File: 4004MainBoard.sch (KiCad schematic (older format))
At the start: 94 parts, among them J1 BUS, J2 P0 RAM1, J3 CMRAM RAM2, J4 P0 RAM2, J5 DC 5V, Q1 2SA1162GR, Q10 2SC2712GR, Q11 2SA1162GR, Q2 2SC2712GR, Q3 2SA1162GR, Q4 2SC2712GR, Q5 2SA1162GR, Q6 2SA1162GR, Q7 2SA1162GR, Q8 2SA1162GR, Q9 2SC2712GR, SW1 TEST, SW2 RESET, SW3 POWER, U1 74HC08, U2 74HC161, U3 PST600, U4 Intel4004, U5 LT1931A, U6 74LS540, U7 Intel4002-1, U8 Intel4002-1, U9 LT1763, Y1 DLO555MB

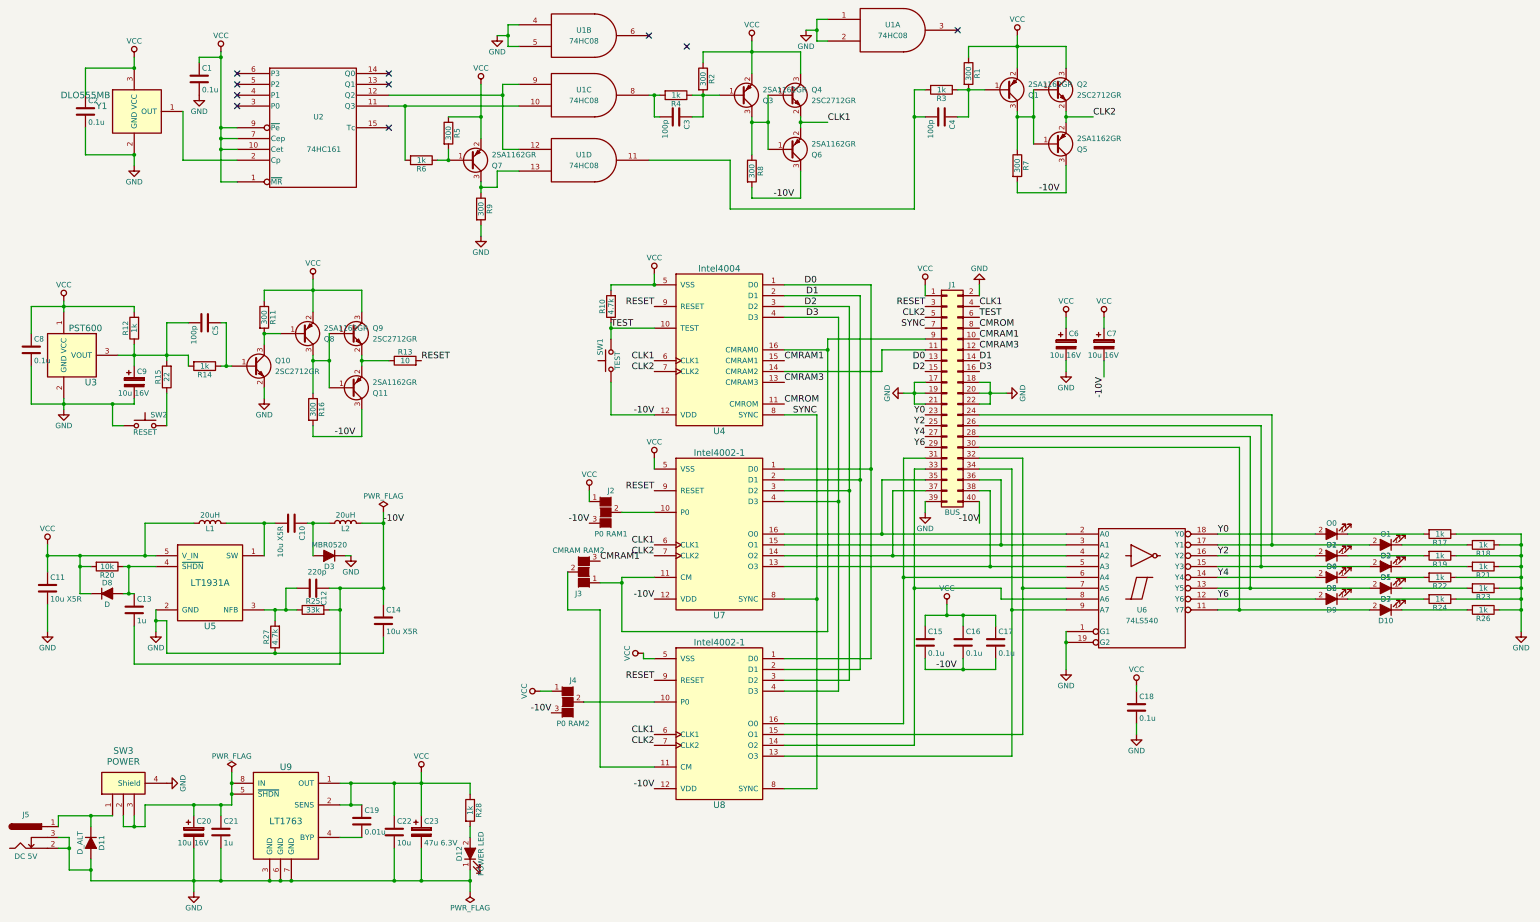
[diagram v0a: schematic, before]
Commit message: パターンを実装
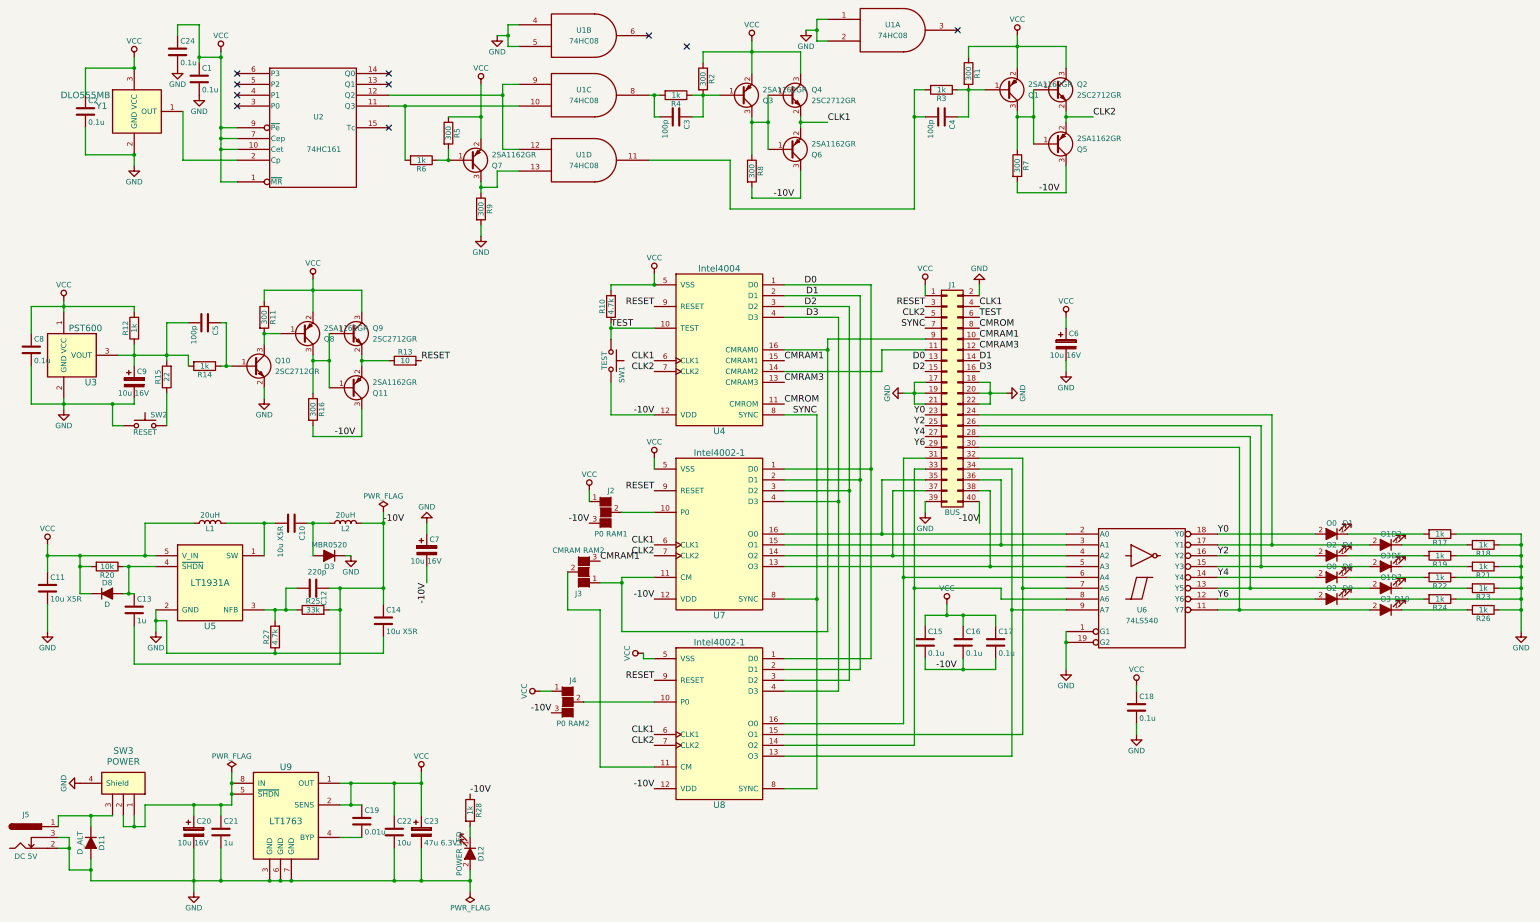
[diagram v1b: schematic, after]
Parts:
- added C24: 0.1u, Capacitors_SMD:C_0603_HandSoldering, symbol C
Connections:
- net -10V: now also R28.1, SW1.2; no longer SW1.1
- net GND: now also C7.1, D12.2 (A), C24.2; no longer D12.1 (K)
- net TEST: now also SW1.1; no longer SW1.2
- net VCC: now also C24.1; no longer C7.1, R28.1
- net at D11.1 (K), J5.1: now also SW3.3; no longer SW3.1
- net at C20.1, C21.1, SW3.2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: now also SW3.1; no longer SW3.3
- net at R28.2: now also D12.1 (K); no longer D12.2 (A)
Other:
- moved on the sheet: C7, D12, SW1, SW3
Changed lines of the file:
@@
 F 3 "" H 2000 8300 60  0001 C CNN
 	1    2000 8300
-	1    0    0    -1
+	-1   0    0    -1
 $EndComp
 $Comp
@@
 L GND #PWR02
 U 1 1 5A62F813
-P 2400 8200
-F 0 "#PWR02" H 2400 7950 50  0001 C CNN
-F 1 "GND" H 2400 8050 50  0000 C CNN
-F 2 "" H 2400 8200 50  0001 C CNN
-F 3 "" H 2400 8200 50  0001 C CNN
-	1    2400 8200
-	0    -1   -1   0
+P 1600 8200
+F 0 "#PWR02" H 1600 7950 50  0001 C CNN
+F 1 "GND" H 1600 8050 50  0000 C CNN
+F 2 "" H 1600 8200 50  0001 C CNN
+F 3 "" H 1600 8200 50  0001 C CNN
+	1    1600 8200
+	0    1    1    0
 $EndComp
 $Comp
@@
 F 3 "" H 5200 8850 50  0001 C CNN
 	1    5200 8850
-	0    -1   -1   0
+	0    1    1    0
 $EndComp
 $Comp
@@
 F 3 "" H 6500 4500 50  0001 C CNN
 	1    6500 4300
-	0    -1   -1   0
+	0    1    1    0
 $EndComp
 Text Label 6500 4000 0    60   ~ 0
@@
 Connection ~ 4500 9100
 Wire Wire Line
-	4000 8200 5200 8200
+	4000 8200 4750 8200
 Wire Wire Line
 	4500 8200 4500 8500
@@
 Wire Wire Line
 	5200 8700 5200 8600
-Wire Wire Line
-	5200 8200 5200 8300
 Wire Wire Line
 	2300 6600 2300 6800
@@
 Connection ~ 2900 2350
 Wire Wire Line
-	2700 1550 2700 1500
+	2700 1200 2700 1550
 Wire Wire Line
 	2700 1500 2900 1500
@@
 U 1 1 5A66297C
 P 13150 5900
-F 0 "D1" H 13150 6000 50  0000 C CNN
+F 0 "D1" H 13000 5800 50  0000 C CNN
 F 1 "O0" H 13150 5800 50  0000 C CNN
 F 2 "LEDs:LED_0603_HandSoldering" H 13150 5900 50  0001 C CNN
@@
 U 1 1 5A662D8D
 P 13150 6100
-F 0 "D4" H 13150 6200 50  0000 C CNN
+F 0 "D4" H 13000 6000 50  0000 C CNN
 F 1 "O2" H 13150 6000 50  0000 C CNN
 F 2 "LEDs:LED_0603_HandSoldering" H 13150 6100 50  0001 C CNN
@@
 U 1 1 5A662EAB
 P 13150 6300
-F 0 "D6" H 13150 6400 50  0000 C CNN
+F 0 "D6" H 13000 6200 50  0000 C CNN
 F 1 "O0" H 13150 6200 50  0000 C CNN
 F 2 "LEDs:LED_0603_HandSoldering" H 13150 6300 50  0001 C CNN
@@
 U 1 1 5A662FC5
 P 13150 6500
-F 0 "D9" H 13150 6600 50  0000 C CNN
+F 0 "D9" H 13000 6400 50  0000 C CNN
 F 1 "O2" H 13150 6400 50  0000 C CNN
 F 2 "LEDs:LED_0603_HandSoldering" H 13150 6500 50  0001 C CNN
@@
 U 1 1 5A663256
 P 13650 6000
-F 0 "D2" H 13650 6100 50  0000 C CNN
+F 0 "D2" H 13550 5900 50  0000 C CNN
 F 1 "O1" H 13650 5900 50  0000 C CNN
 F 2 "LEDs:LED_0603_HandSoldering" H 13650 6000 50  0001 C CNN
@@
 U 1 1 5A66337A
 P 13650 6200
-F 0 "D5" H 13650 6300 50  0000 C CNN
+F 0 "D5" H 13550 6100 50  0000 C CNN
 F 1 "O3" H 13650 6100 50  0000 C CNN
 F 2 "LEDs:LED_0603_HandSoldering" H 13650 6200 50  0001 C CNN
@@
 U 1 1 5A66349C
 P 13650 6400
-F 0 "D7" H 13650 6500 50  0000 C CNN
+F 0 "D7" H 13550 6300 50  0000 C CNN
 F 1 "O1" H 13650 6300 50  0000 C CNN
 F 2 "LEDs:LED_0603_HandSoldering" H 13650 6400 50  0001 C CNN
@@
 U 1 1 5A6635C2
 P 13650 6600
-F 0 "D10" H 13650 6700 50  0000 C CNN
+F 0 "D10" H 13500 6500 50  0000 C CNN
 F 1 "O3" H 13650 6500 50  0000 C CNN
 F 2 "LEDs:LED_0603_HandSoldering" H 13650 6600 50  0001 C CNN
@@
 L CP C7
 U 1 1 5A66BB0D
-P 11050 4150
-F 0 "C7" H 11075 4250 50  0000 L CNN
-F 1 "10u 16V" H 10900 4050 50  0000 L CNN
-F 2 "Capacitors_SMD:CP_Elec_4x4.5" H 11088 4000 50  0001 C CNN
-F 3 "" H 11050 4150 50  0001 C CNN
-	1    11050 4150
-	1    0    0    -1
-$EndComp
-$Comp
-L VCC #PWR037
-U 1 1 5A66BC40
-P 11050 3900
-F 0 "#PWR037" H 11050 3750 50  0001 C CNN
-F 1 "VCC" H 11050 4050 50  0000 C CNN
-F 2 "" H 11050 3900 50  0001 C CNN
-F 3 "" H 11050 3900 50  0001 C CNN
-	1    11050 3900
-	1    0    0    -1
-$EndComp
-Text Label 11050 4450 3    60   ~ 0
+P 4800 6050
+F 0 "C7" H 4825 6150 50  0000 L CNN
+F 1 "10u 16V" H 4650 5950 50  0000 L CNN
+F 2 "Capacitors_SMD:CP_Elec_4x4.5" H 4838 5900 50  0001 C CNN
+F 3 "" H 4800 6050 50  0001 C CNN
+	1    4800 6050
+	1    0    0    -1
+$EndComp
+Text Label 4800 6350 3    60   ~ 0
 -10V
 Wire Wire Line
-	11050 4300 11050 4450
-Wire Wire Line
-	11050 4000 11050 3900
-$Comp
-L PWR_FLAG #FLG038
+	4800 6200 4800 6350
+Wire Wire Line
+	4800 5900 4800 5800
+$Comp
+L PWR_FLAG #FLG037
 U 1 1 5A66F18F
 P 5200 9200
-F 0 "#FLG038" H 5200 9275 50  0001 C CNN
+F 0 "#FLG037" H 5200 9275 50  0001 C CNN
 F 1 "PWR_FLAG" H 5200 9350 50  0000 C CNN
 F 2 "" H 5200 9200 50  0001 C CNN
@@
 $EndComp
 $Comp
-L PWR_FLAG #FLG039
+L PWR_FLAG #FLG038
 U 1 1 5A66F31E
 P 4400 5700
-F 0 "#FLG039" H 4400 5775 50  0001 C CNN
+F 0 "#FLG038" H 4400 5775 50  0001 C CNN
 F 1 "PWR_FLAG" H 4400 5850 50  0000 C CNN
 F 2 "" H 4400 5700 50  0001 C CNN
@@
 Connection ~ 5200 9100
 $Comp
-L PWR_FLAG #FLG040
+L PWR_FLAG #FLG039
 U 1 1 5A66FDA3
 P 3000 8100
-F 0 "#FLG040" H 3000 8175 50  0001 C CNN
+F 0 "#FLG039" H 3000 8175 50  0001 C CNN
 F 1 "PWR_FLAG" H 3000 8250 50  0000 C CNN
 F 2 "" H 3000 8100 50  0001 C CNN
@@
 Connection ~ 10000 4600
 $Comp
-L GND #PWR041
+L GND #PWR040
 U 1 1 5A67152F
 P 9200 4600
-F 0 "#PWR041" H 9200 4350 50  0001 C CNN
+F 0 "#PWR040" H 9200 4350 50  0001 C CNN
 F 1 "GND" H 9200 4450 50  0000 C CNN
 F 2 "" H 9200 4600 50  0001 C CNN
@@
 $EndComp
 $Comp
-L GND #PWR042
+L GND #PWR041
 U 1 1 5A67165D
 P 10150 4600
-F 0 "#PWR042" H 10150 4350 50  0001 C CNN
+F 0 "#PWR041" H 10150 4350 50  0001 C CNN
 F 1 "GND" H 10150 4450 50  0000 C CNN
 F 2 "" H 10150 4600 50  0001 C CNN
@@
 	0    -1   -1   0
 $EndComp
+$Comp
+L GND #PWR042
+U 1 1 5A6475BE
+P 4800 5800
+F 0 "#PWR042" H 4800 5550 50  0001 C CNN
+F 1 "GND" H 4800 5650 50  0000 C CNN
+F 2 "" H 4800 5800 50  0001 C CNN
+F 3 "" H 4800 5800 50  0001 C CNN
+	1    4800 5800
+	-1   0    0    1
+$EndComp
+$Comp
+L C C24
+U 1 1 5A648DDE
+P 2500 1450
+F 0 "C24" H 2525 1550 50  0000 L CNN
+F 1 "0.1u" H 2525 1350 50  0000 L CNN
+F 2 "Capacitors_SMD:C_0603_HandSoldering" H 2538 1300 50  0001 C CNN
+F 3 "" H 2500 1450 50  0001 C CNN
+	1    2500 1450
+	1    0    0    -1
+$EndComp
+$Comp
+L GND #PWR043
+U 1 1 5A649039
+P 2500 1600
+F 0 "#PWR043" H 2500 1350 50  0001 C CNN
+F 1 "GND" H 2500 1450 50  0000 C CNN
+F 2 "" H 2500 1600 50  0001 C CNN
+F 3 "" H 2500 1600 50  0001 C CNN
+	1    2500 1600
+	1    0    0    -1
+$EndComp
+Wire Wire Line
+	2500 1300 2500 1200
+Wire Wire Line
+	2500 1200 2700 1200
+Connection ~ 2700 1500
+Text Label 5200 8300 0    60   ~ 0
+-10V
 $EndSCHEMATC

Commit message: パターン修正 ビア実装
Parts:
- added R29, R30: 22, Resistors_SMD:R_0603_HandSoldering, symbol R
- added R31, R32, R33, R34: 22k, Resistors_SMD:R_0603_HandSoldering, symbol R
- D12: value POWER LED -> POWER
- R13: value 10 -> 22
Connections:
- net CLK1: now also R30.2; no longer Q4.2 (E), Q6.2 (E)
- net CLK2: now also R29.2; no longer Q2.2 (E), Q5.2 (E)
- net D0: now also R34.2
- net D1: now also R33.2
- net D2: now also R32.2
- net D3: now also R31.2
- net VCC: now also R31.1, R32.1, R33.1, R34.1
- new net: Q4.2 (E), Q6.2 (E), R30.1
- new net: Q2.2 (E), Q5.2 (E), R29.1
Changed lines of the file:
@@
 P 5200 8850
 F 0 "D12" H 5200 8950 50  0000 C CNN
-F 1 "POWER LED" H 5200 8750 50  0000 C CNN
+F 1 "POWER" H 5200 8750 50  0000 C CNN
 F 2 "LEDs:LED_0603_HandSoldering" H 5200 8850 50  0001 C CNN
 F 3 "" H 5200 8850 50  0001 C CNN
@@
 Text Label 8000 2800 0    60   ~ 0
 -10V
-Text Label 8500 2100 0    60   ~ 0
+Text Label 8800 2100 0    60   ~ 0
 CLK1
 $Comp
@@
 Text Label 10450 2750 0    60   ~ 0
 -10V
-Text Label 10950 2050 0    60   ~ 0
+Text Label 11250 2050 0    60   ~ 0
 CLK2
 Text Label 4750 4300 0    60   ~ 0
@@
 P 4600 4300
 F 0 "R13" V 4680 4300 50  0000 C CNN
-F 1 "10" V 4600 4300 50  0000 C CNN
+F 1 "22" V 4600 4300 50  0000 C CNN
 F 2 "Resistors_SMD:R_0603_HandSoldering" V 4530 4300 50  0001 C CNN
 F 3 "" H 4600 4300 50  0001 C CNN
@@
 	8100 3900 8600 3900
 Wire Wire Line
-	8600 3900 8600 7350
+	8600 3500 8600 7350
 Wire Wire Line
 	8600 5600 8100 5600
@@
 	8100 5500 8700 5500
 Wire Wire Line
-	8700 3800 8700 7250
+	8700 3500 8700 7250
 Wire Wire Line
 	8700 3800 8100 3800
@@
 	8100 5400 8800 5400
 Wire Wire Line
-	8800 3700 8800 7150
+	8800 3500 8800 7150
 Wire Wire Line
 	8800 3700 8100 3700
@@
 	8100 5300 8900 5300
 Wire Wire Line
-	8900 3600 8900 7050
+	8900 3500 8900 7050
 Wire Wire Line
 	8900 3600 8100 3600
@@
 Text Label 5200 8300 0    60   ~ 0
 -10V
+$Comp
+L R R30
+U 1 1 5AEC6C94
+P 8650 2100
+F 0 "R30" V 8730 2100 50  0000 C CNN
+F 1 "22" V 8650 2100 50  0000 C CNN
+F 2 "Resistors_SMD:R_0603_HandSoldering" V 8580 2100 50  0001 C CNN
+F 3 "" H 8650 2100 50  0001 C CNN
+	1    8650 2100
+	0    -1   -1   0
+$EndComp
+$Comp
+L R R29
+U 1 1 5AEC6F5E
+P 11100 2050
+F 0 "R29" V 11180 2050 50  0000 C CNN
+F 1 "22" V 11100 2050 50  0000 C CNN
+F 2 "Resistors_SMD:R_0603_HandSoldering" V 11030 2050 50  0001 C CNN
+F 3 "" H 11100 2050 50  0001 C CNN
+	1    11100 2050
+	0    -1   -1   0
+$EndComp
+$Comp
+L R R31
+U 1 1 5AEC8B2E
+P 8600 3350
+F 0 "R31" V 8680 3350 50  0000 C CNN
+F 1 "22k" V 8600 3350 50  0000 C CNN
+F 2 "Resistors_SMD:R_0603_HandSoldering" V 8530 3350 50  0001 C CNN
+F 3 "" H 8600 3350 50  0001 C CNN
+	1    8600 3350
+	1    0    0    -1
+$EndComp
+$Comp
+L R R32
+U 1 1 5AEC8D49
+P 8700 3350
+F 0 "R32" V 8780 3350 50  0000 C CNN
+F 1 "22k" V 8700 3350 50  0000 C CNN
+F 2 "Resistors_SMD:R_0603_HandSoldering" V 8630 3350 50  0001 C CNN
+F 3 "" H 8700 3350 50  0001 C CNN
+	1    8700 3350
+	1    0    0    -1
+$EndComp
+$Comp
+L R R33
+U 1 1 5AEC8E8A
+P 8800 3350
+F 0 "R33" V 8880 3350 50  0000 C CNN
+F 1 "22k" V 8800 3350 50  0000 C CNN
+F 2 "Resistors_SMD:R_0603_HandSoldering" V 8730 3350 50  0001 C CNN
+F 3 "" H 8800 3350 50  0001 C CNN
+	1    8800 3350
+	1    0    0    -1
+$EndComp
+$Comp
+L R R34
+U 1 1 5AEC8FCD
+P 8900 3350
+F 0 "R34" V 8980 3350 50  0000 C CNN
+F 1 "22k" V 8900 3350 50  0000 C CNN
+F 2 "Resistors_SMD:R_0603_HandSoldering" V 8830 3350 50  0001 C CNN
+F 3 "" H 8900 3350 50  0001 C CNN
+	1    8900 3350
+	1    0    0    -1
+$EndComp
+$Comp
+L VCC #PWR044
+U 1 1 5AEC9330
+P 8500 3100
+F 0 "#PWR044" H 8500 2950 50  0001 C CNN
+F 1 "VCC" H 8500 3250 50  0000 C CNN
+F 2 "" H 8500 3100 50  0001 C CNN
+F 3 "" H 8500 3100 50  0001 C CNN
+	1    8500 3100
+	1    0    0    -1
+$EndComp
+Wire Wire Line
+	8500 3100 8500 3150
+Wire Wire Line
+	8500 3150 8900 3150
+Wire Wire Line
+	8900 3150 8900 3200
+Wire Wire Line
+	8800 3200 8800 3150
+Connection ~ 8800 3150
+Wire Wire Line
+	8700 3200 8700 3150
+Connection ~ 8700 3150
+Wire Wire Line
+	8600 3200 8600 3150
+Connection ~ 8600 3150
+Connection ~ 8600 3900
+Connection ~ 8700 3800
+Connection ~ 8800 3700
+Connection ~ 8900 3600
 $EndSCHEMATC
